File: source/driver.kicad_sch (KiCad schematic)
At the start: 49 parts, among them U2 IRS21867S, U3 IRS21867S, U4 IRS21867S, U5 TX4130L/PW2902

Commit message: Add files via upload
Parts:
- renumbered C17 to C13, C18 to C14, C19 to C15, C20 to C16, C21 to C17, C22 to C18, C23 to C19
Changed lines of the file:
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@@
   (symbol (lib_id "Device:C") (at 270.51 128.27 0) (unit 1)
     (in_bom yes) (on_board yes)
-    (property "Reference" "C22" (id 0) (at 270.51 125.73 0)
+    (property "Reference" "C18" (id 0) (at 270.51 125.73 0)
       (effects (font (size 1.27 1.27)) (justify left))
     )
@@
   (symbol (lib_id "BLDC_4-rescue:C-RESCUE-BLDC_4") (at 199.39 148.59 180) (unit 1)
     (in_bom yes) (on_board yes)
-    (property "Reference" "C18" (id 0) (at 199.39 151.13 0)
+    (property "Reference" "C14" (id 0) (at 199.39 151.13 0)
       (effects (font (size 1.27 1.27)) (justify left))
     )
@@
   (symbol (lib_id "Custom_Library:C_T491D107K016AT") (at 276.86 128.27 0) (unit 1)
     (in_bom yes) (on_board yes) (fields_autoplaced)
-    (property "Reference" "C23" (id 0) (at 280.67 126.3649 0)
+    (property "Reference" "C19" (id 0) (at 280.67 126.3649 0)
       (effects (font (size 1.27 1.27)) (justify left))
     )
@@
   (symbol (lib_id "Device:C") (at 170.18 53.34 0) (unit 1)
     (in_bom yes) (on_board yes)
-    (property "Reference" "C17" (id 0) (at 171.45 50.8 0)
+    (property "Reference" "C13" (id 0) (at 171.45 50.8 0)
       (effects (font (size 1.27 1.27)) (justify left))
     )
@@
   (symbol (lib_id "BLDC_4-rescue:C-RESCUE-BLDC_4") (at 233.68 138.43 270) (unit 1)
     (in_bom yes) (on_board yes)
-    (property "Reference" "C20" (id 0) (at 234.95 137.16 90)
+    (property "Reference" "C16" (id 0) (at 234.95 137.16 90)
       (effects (font (size 1.27 1.27)) (justify left))
     )
@@
   (symbol (lib_id "Device:C") (at 204.47 50.8 0) (unit 1)
     (in_bom yes) (on_board yes)
-    (property "Reference" "C19" (id 0) (at 204.47 48.26 0)
+    (property "Reference" "C15" (id 0) (at 204.47 48.26 0)
       (effects (font (size 1.27 1.27)) (justify left))
     )
@@
   (symbol (lib_id "Device:C") (at 264.16 128.27 0) (unit 1)
     (in_bom yes) (on_board yes)
-    (property "Reference" "C21" (id 0) (at 264.16 125.73 0)
-      (effects (font (size 1.27 1.27)) (justify left))
-    )
+    (property "Reference" "C17" (id 0) (at 264.16 125.73 0)
+      (effects (font (size 1.27 1.27)) (justify left))
+    )

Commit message: Add files via upload
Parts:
- removed C10, C12: 10u @ 50V, Capacitor_SMD:C_1206_3216Metric, symbol Device:C
- added C12, C3, C8: 10u, Capacitor_Tantalum_SMD:CP_EIA-3216-10_Kemet-I, symbol Device:C_Polarized_Small
- C10: renamed from C8; value 100n -> 1u; LCSC C14663 -> C15849
- C11: renamed from C9; value 10u @ 50V -> 10u @ 100V; footprint Capacitor_SMD:C_1206_3216Metric -> Capacitor_SMD:C_2220_5650Metric; LCSC C13585 -> C2843466
- C13: renamed from C11; value 10u @ 50V -> 10u @ 100V; footprint Capacitor_SMD:C_1206_3216Metric -> Capacitor_SMD:C_2220_5650Metric; LCSC C13585 -> C2843466
- C16: renamed from C15; value 100n -> 1u; LCSC C14663 -> C15849
- C6: renamed from C5; value 100n -> 1u; LCSC C14663 -> C15849
- renumbered C13 to C14, C14 to C15, C16 to C17, C17 to C18, C18 to C19, C19 to C20, C3 to C4, C4 to C5, C6 to C7, C7 to C9
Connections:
- net +12V: now also C12.1, C3.1, C8.1
- net GND: now also C11.1, C13.2, C12.2, C3.2, C8.2
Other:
- note added: "WATT'EVER"
- note removed: "F-Of-C"

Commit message: Add files via upload
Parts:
- removed C11: 10u @ 100V, Capacitor_SMD:C_2220_5650Metric, symbol Device:C
- renumbered C9 to C10, C10 to C11, C3 to C4, C4 to C5, C5 to C6, C6 to C7, C7 to C8, C8 to C9, R6 to R10, R7 to R11, R8 to R12, R9 to R13, R10 to R14, R11 to R15, R12 to R16, R13 to R17, R14 to R18, R15 to R19, R16 to R20, R17 to R21, R18 to R22, R19 to R23, R20 to R24, R3 to R7, R4 to R8, R5 to R9
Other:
- note removed: "combined: 20uF @ 100v"

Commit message: Add files via upload
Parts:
- removed D2, D4, D8: 1N4148WS, Diode_SMD:D_SOD-323, symbol Diode:1N4148W
- removed R19, R9: 2R, Resistor_SMD:R_0603_1608Metric, symbol Device:R
- added C10, C17, C22: 1n, Capacitor_SMD:C_0603_1608Metric, symbol Device:C
- added C11, C21: 100u@6.3V, Capacitor_SMD:C_1206_3216Metric, symbol Device:C
- added C15, C20, C9: 15n, Capacitor_SMD:C_0603_1608Metric, symbol Device:C
- added C19: 100u, Capacitor_Tantalum_SMD:CP_EIA-3528-21_Kemet-B, symbol Custom_Library:C_T491D107K016AT
- added C6: 100n, Capacitor_SMD:C_0603_1608Metric, symbol BLDC_4-rescue:C-RESCUE-BLDC_4
- added CYA0650-68UH1: 68uH, Custom:L_6.6x7.2_H5.0_CYA0650_68UH, symbol pspice:INDUCTOR
- added D2: 1N5819, Diode_SMD:D_SOD-323, symbol Diode:1N5819
- added R10, R11: 1k, Resistor_SMD:R_0603_1608Metric, symbol Device:R
- added U2: AMS1117-3.3, Package_TO_SOT_SMD:SOT-223-3_TabPin2, symbol Regulator_Linear:LM1117-3.3
- added U3, U5, U8: MC74VHC1G66, Package_TO_SOT_SMD:SOT-353_SC-70-5, symbol 74xGxx:74AHC1G4210
- added U6: XL1509-5.0E1, Package_SO:SOP-8_3.9x4.9mm_P1.27mm, symbol Custom_Library:XL1509-5.0E1
- R14: value 2R -> 1k; LCSC C22977 -> C22975
- U4: renamed from U2; value IRS21867S -> EG3112; LCSC C52290 -> C111908
- U7: renamed from U3; value IRS21867S -> EG3112; LCSC C52290 -> C111908
- U9: renamed from U4; value IRS21867S -> EG3112; LCSC C52290 -> C111908
- renumbered C7 to C12, C6 to C13, C9 to C14, C10 to C16, C11 to C18, C12 to C23, C14 to C24, C13 to C25, C15 to C26, C16 to C27, C17 to C28, C18 to C29, C19 to C30, C20 to C31, C4 to C5, C5 to C7, CYA0650-68UH1 to CYA0650-68UH2, D5 to D4, D6 to D5, D7 to D6, D9 to D7, R20 to R19, R21 to R20, R22 to R21, R23 to R22, R24 to R23, R10 to R24, R11 to R25, R7 to R8, R8 to R9, U5 to U10
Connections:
- net +12V: now also U6.1 (Vin), U6.4 (O/O)
- net GND: now also C10.2, C11.2, C15.2, C17.2, C19.2, C20.2, C21.2, C22.2, C6.1, C9.2, D2.2 (A), U2.1 (GND), U3.3 (GND), U5.3 (GND), U6.5 (GND), U6.6 (GND), U6.7 (GND), U6.8 (GND), U8.3 (GND); no longer C14.2, C16.2
- net HS1: now also C12.2, U4.6 (VS)
- net HS2: now also C18.2, U7.6 (VS); no longer R14.2
- net HS3: now also C27.2, U9.6 (VS)
- net VCC: now also C11.1, U2.2 (VO), U3.5 (VCC), U5.5 (VCC), U8.5 (VCC)
- new net: C20.1, U8.2 (X2)
- new net: C15.1, U5.2 (X2)
- new net: CYA0650-68UH1.1, D2.1 (K), U6.2 (Vout)
- new net: C9.1, U3.2 (X2)
- new net: C14.2, C16.2
- new net +5V: C19.1, C21.1, C6.2, CYA0650-68UH1.2, U2.3 (VI), U6.3 (FB)
- new net CURR_A: C10.1, R10.1, U3.1 (X1)
- new net CURR_B: C17.1, R11.1, U5.1 (X1)
- new net CURR_C: C22.1, R14.1, U8.1 (X1)
- new net CURR_FILTER: U3.4 (Q), U5.4 (Q), U8.4 (Q)
- new net C_A: R10.2
- new net C_B: R11.2
- new net C_C: R14.2
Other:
- note added: "BOARD REGULATOR"
- note added: "PCB Layout Tips (Gate Driver) Distance between high and low voltage components: It's strongly recommended to place the components tied to the floating voltage pins (VB and VS) near the respective high voltage portions of the device. Please see the Case Outline information in this datasheet for the details. Ground Plane: In order to minimize noise coupling, the ground plane should not be placed un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"
- note added: "Power stage PCB parasitic elements can contribute to large negative voltage transients at the switch node; it is recommended to limit the phase voltage negative transients. In order to avoid such conditions, it is recommended to 1) minimize the high-side emitter to low-side collector distance, and 2) minimize the low-side emitter to negative bus rail stray inductance. However, where negative VS s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"
- moved on the sheet: C13, C25, C8, R12, R13, R16, R17, R24, R25, R8, R9

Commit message: Add files via upload
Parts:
- removed C10, C22: 1n, Capacitor_SMD:C_0603_1608Metric, symbol Device:C
- removed C15, C20: 15n, Capacitor_SMD:C_0603_1608Metric, symbol Device:C
- removed R10, R11, R14: 1k, Resistor_SMD:R_0603_1608Metric, symbol Device:R
- added C14: 100n, Capacitor_SMD:C_0603_1608Metric, symbol Device:C
- C17: value 1n -> 100n; LCSC C23630 -> C14663
- C9: value 15n -> 100n; LCSC C23630 -> C14663
- U3, U5, U8: LCSC (none) -> C233641
- renumbered C11 to C10, C12 to C11, C13 to C12, C14 to C13, C16 to C15, C18 to C16, C19 to C18, C21 to C19, C23 to C20, C24 to C21, C25 to C22, C26 to C23, C27 to C24, C28 to C25, C29 to C26, C30 to C27, C31 to C28, R12 to R10, R13 to R11, R16 to R12, R17 to R13, R15 to R14, R18 to R15, R19 to R16, R20 to R17, R21 to R18, R22 to R19, R23 to R20, R24 to R21, R25 to R22
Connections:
- net GND: now also U3.2 (X2), U5.2 (X2), U8.2 (X2); no longer C17.2, C9.2
- net SENS_1: now also C9.1
- net SENS_2: now also C14.1
- net SENS_3: now also C17.1
- net CURR_A: no longer names the net of U3.1 (X1)
- net CURR_A: now also C9.2
- net CURR_B: no longer names the net of U5.1 (X1)
- net CURR_B: now also C14.2; no longer C17.1
- net CURR_C: no longer names the net of U8.1 (X1)
- net CURR_C: now also C17.2
- net CURR_FILTER renamed SENS_FILTER
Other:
- note added: "FOC KING"
- note added: "ON/OFF Voltage Filters"
- note removed: "WATT'EVER"
- moved on the sheet: R10, R11, R12, R13, R8, R9, U3

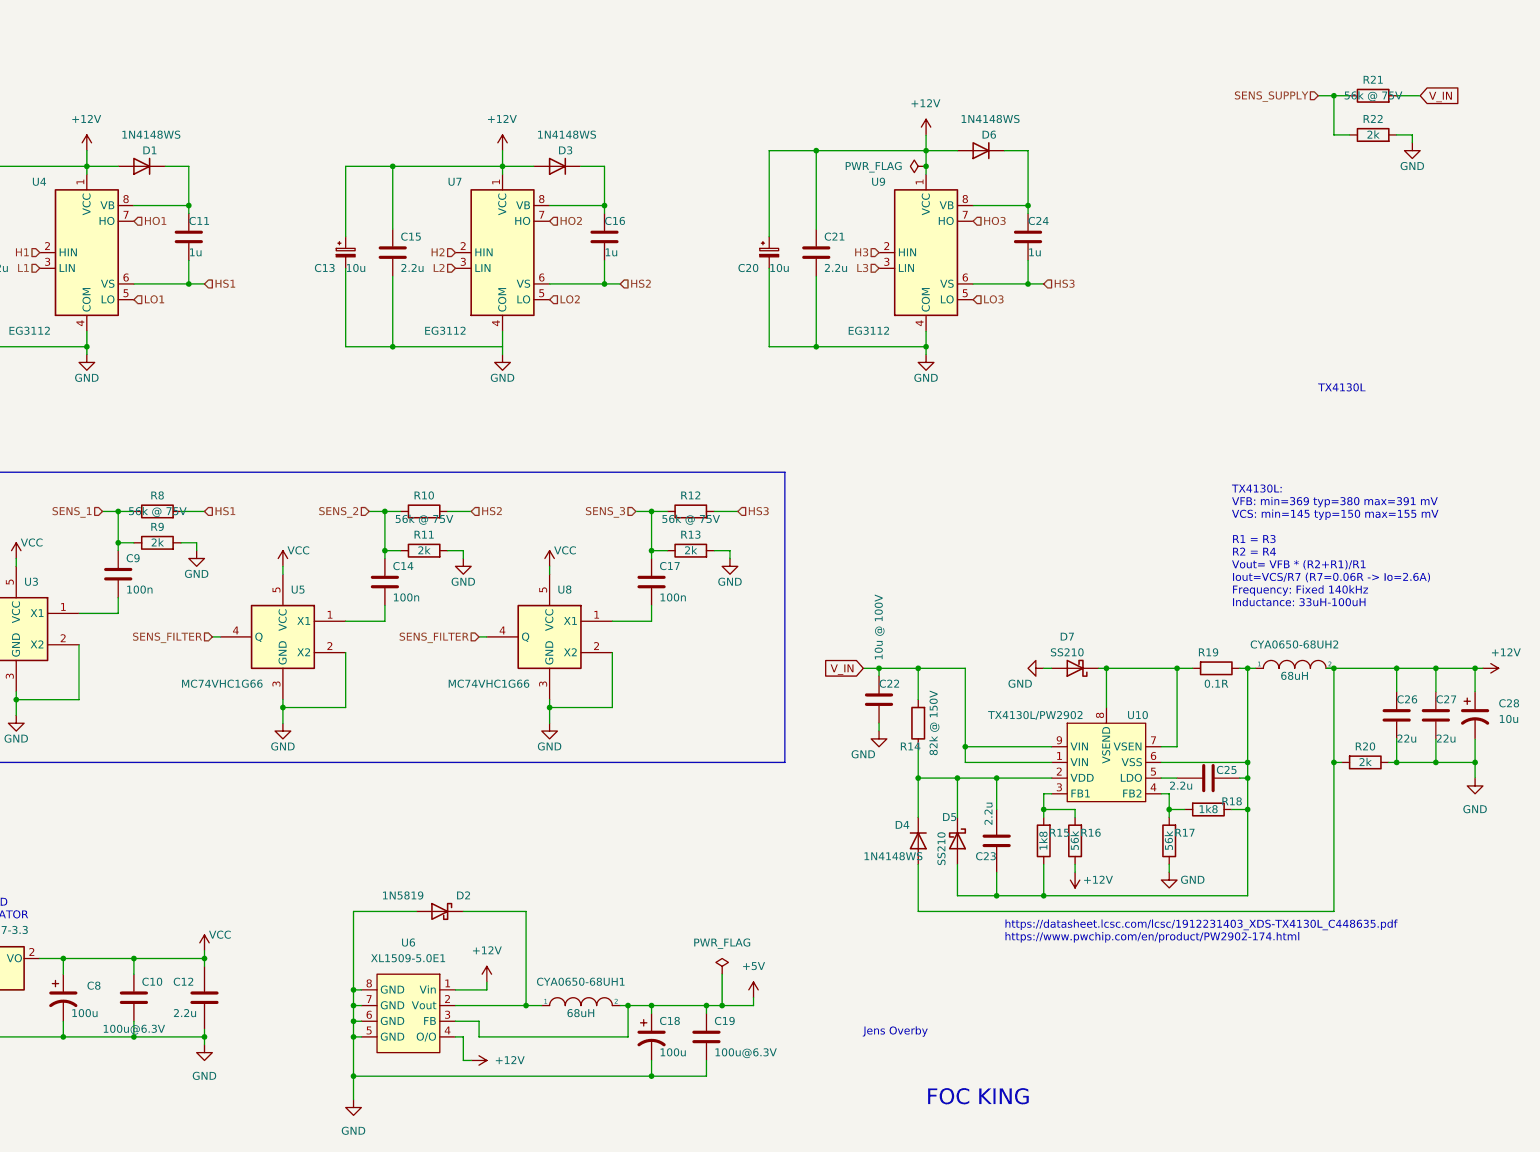
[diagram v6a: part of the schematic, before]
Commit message: 4 layer design
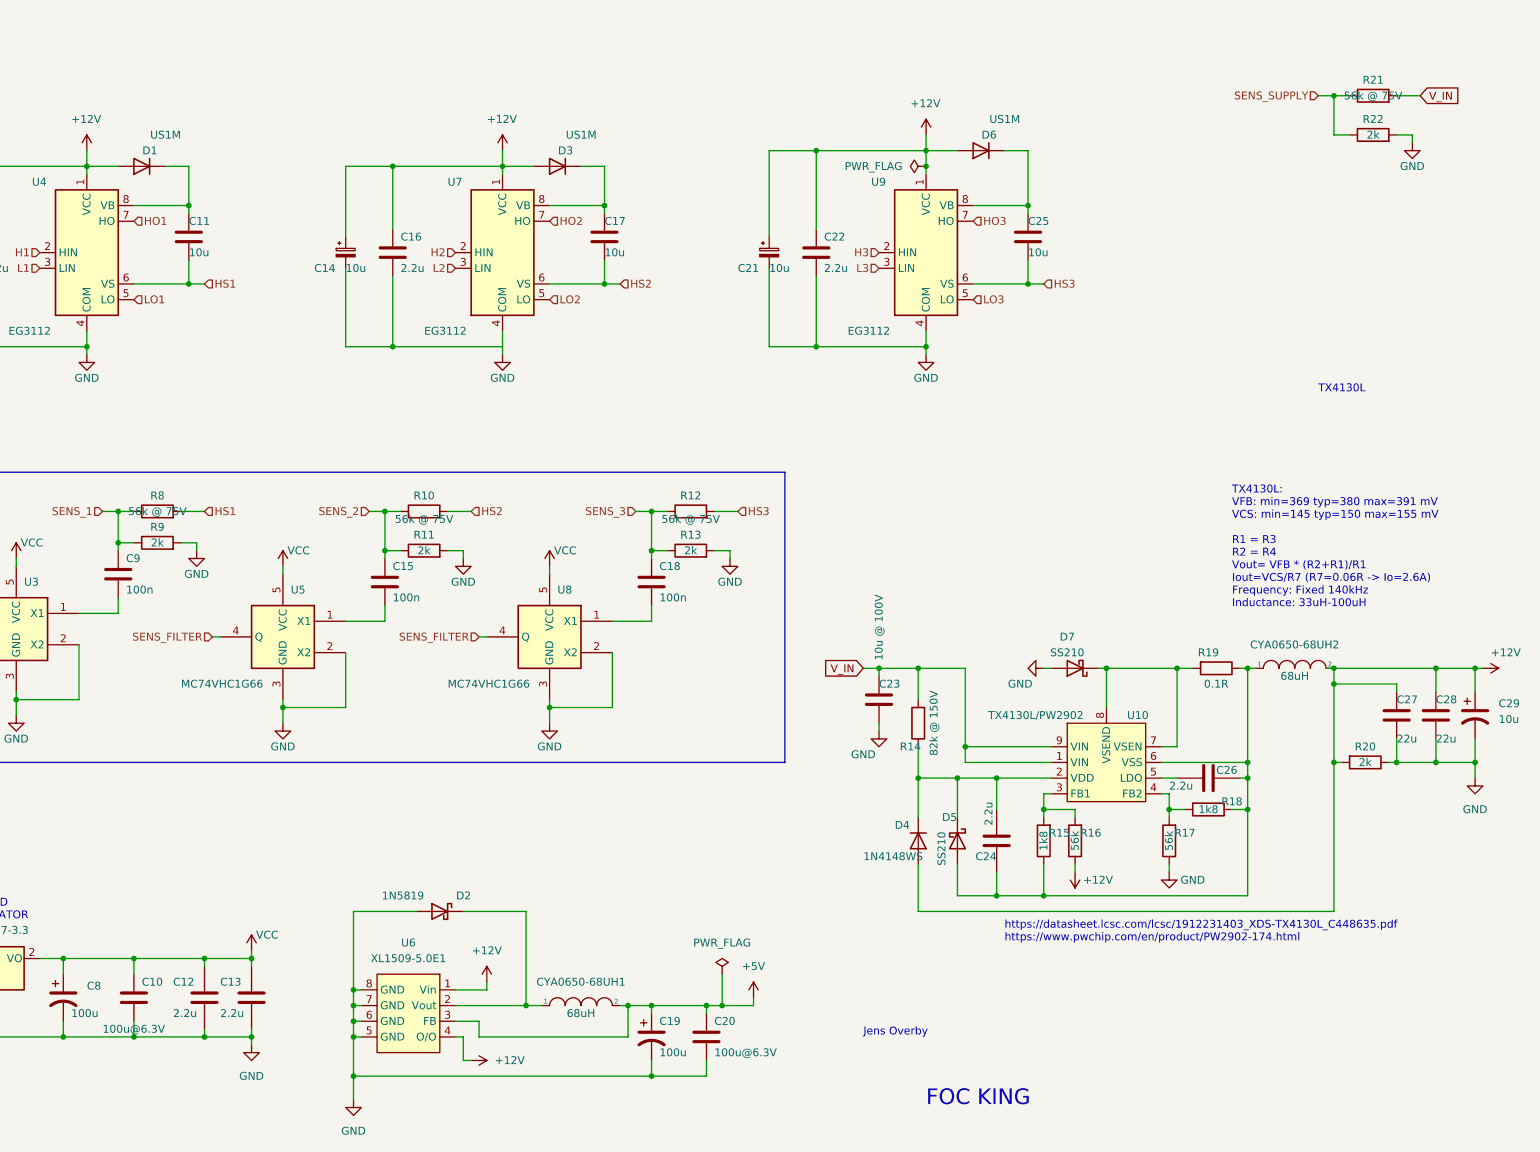
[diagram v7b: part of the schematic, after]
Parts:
- added C12: 2.2u, Capacitor_SMD:C_0603_1608Metric, symbol BLDC_4-rescue:C-RESCUE-BLDC_4
- C11: value 1u -> 10u; LCSC C15849 -> C96446
- C17: renamed from C16; value 1u -> 10u; LCSC C15849 -> C96446
- C25: renamed from C24; value 1u -> 10u; LCSC C15849 -> C96446
- D1, D3, D6: value 1N4148WS -> US1M; footprint Diode_SMD:D_SOD-323 -> Diode_SMD:D_SMA; LCSC C2128 -> C412437
- renumbered C12 to C13, C13 to C14, C14 to C15, C15 to C16, C17 to C18, C18 to C19, C19 to C20, C20 to C21, C21 to C22, C22 to C23, C23 to C24, C25 to C26, C26 to C27, C27 to C28, C28 to C29
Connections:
- net GND: now also C12.2
- net VCC: now also C12.1
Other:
- moved on the sheet: C13

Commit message: Add files via upload
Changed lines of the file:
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@@
   (junction (at 186.69 138.43) (diameter 0) (color 0 0 0 0)
   )
+  (junction (at 171.45 161.29) (diameter 0) (color 0 0 0 0)
+  )
   (wire (pts (xy 195.58 58.42) (xy 204.47 58.42))
     (stroke (width 0) (type default) (color 0 0 0 0))
@@
     (stroke (width 0) (type default) (color 0 0 0 0))
   )
+  (wire (pts (xy 171.45 165.1) (xy 171.45 161.29))
+    (stroke (width 0) (type default) (color 0 0 0 0))
+  )
   (wire (pts (xy 96.52 180.34) (xy 95.25 180.34))
     (stroke (width 0) (type default) (color 0 0 0 0))
@@
     (stroke (width 0) (type default) (color 0 0 0 0))
   )
+  (wire (pts (xy 227.33 161.29) (xy 171.45 161.29))
+    (stroke (width 0) (type default) (color 0 0 0 0))
+  )
   (wire (pts (xy 101.6 39.37) (xy 101.6 49.53))
     (stroke (width 0) (type default) (color 0 0 0 0))
@@
     (stroke (width 0) (type default) (color 0 0 0 0))
   )
-  (wire (pts (xy 227.33 152.4) (xy 227.33 153.67))
+  (wire (pts (xy 227.33 152.4) (xy 227.33 161.29))
     (stroke (width 0) (type default) (color 0 0 0 0))
   )
@@
     (stroke (width 0) (type default) (color 0 0 0 0))
   )
+  (wire (pts (xy 171.45 129.54) (xy 180.34 129.54))
+    (stroke (width 0) (type default) (color 0 0 0 0))
+  )
   (wire (pts (xy 240.03 138.43) (xy 240.03 135.89))
     (stroke (width 0) (type default) (color 0 0 0 0))
@@
     (stroke (width 0) (type default) (color 0 0 0 0))
   )
-  (wire (pts (xy 180.34 130.81) (xy 180.34 129.54))
+  (wire (pts (xy 171.45 161.29) (xy 171.45 129.54))
     (stroke (width 0) (type default) (color 0 0 0 0))
   )
@@
   (symbol (lib_id "power:+12V") (at 278.13 120.65 270) (mirror x) (unit 1)
     (in_bom yes) (on_board yes)
-    (property "Reference" "#PWR049" (id 0) (at 274.32 120.65 0)
+    (property "Reference" "#PWR048" (id 0) (at 274.32 120.65 0)
       (effects (font (size 1.27 1.27)) hide)
     )
@@
   (symbol (lib_id "power:GND") (at 276.86 138.43 0) (unit 1)
     (in_bom yes) (on_board yes)
-    (property "Reference" "#PWR048" (id 0) (at 276.86 144.78 0)
+    (property "Reference" "#PWR047" (id 0) (at 276.86 144.78 0)
       (effects (font (size 1.27 1.27)) hide)
     )
@@
   (symbol (lib_id "power:GND") (at 266.7 35.56 0) (unit 1)
     (in_bom yes) (on_board yes)
-    (property "Reference" "#PWR047" (id 0) (at 266.7 41.91 0)
+    (property "Reference" "#PWR046" (id 0) (at 266.7 41.91 0)
       (effects (font (size 1.27 1.27)) hide)
     )
@@
     (pin "1")
   )
-  (symbol (lib_id "power:GND") (at 227.33 153.67 0) (unit 1)
-    (in_bom yes) (on_board yes)
-    (property "Reference" "#PWR046" (id 0) (at 227.33 160.02 0)
-      (effects (font (size 1.27 1.27)) hide)
-    )
-    (property "Value" "GND" (id 1) (at 231.14 154.94 0))
-    (property "Footprint" "" (id 2) (at 227.33 153.67 0)
-      (effects (font (size 1.27 1.27)) hide)
-    )
-    (property "Datasheet" "" (id 3) (at 227.33 153.67 0)
-      (effects (font (size 1.27 1.27)) hide)
-    )
-    (pin "1")
-  )
   (symbol (lib_id "Device:C_Polarized_Small") (at 93.98 53.34 0) (unit 1)
     (in_bom yes) (on_board yes)
@@
     (pin "1")
   )
-  (symbol (lib_id "power:GND") (at 180.34 130.81 0) (unit 1)
+  (symbol (lib_id "power:GND") (at 171.45 165.1 0) (unit 1)
     (in_bom yes) (on_board yes)
-    (property "Reference" "#PWR041" (id 0) (at 180.34 137.16 0)
+    (property "Reference" "#PWR041" (id 0) (at 171.45 171.45 0)
       (effects (font (size 1.27 1.27)) hide)
     )
-    (property "Value" "GND" (id 1) (at 177.8 134.62 0))
-    (property "Footprint" "" (id 2) (at 180.34 130.81 0)
+    (property "Value" "GND" (id 1) (at 168.91 168.91 0))
+    (property "Footprint" "" (id 2) (at 171.45 165.1 0)
       (effects (font (size 1.27 1.27)) hide)
     )
-    (property "Datasheet" "" (id 3) (at 180.34 130.81 0)
+    (property "Datasheet" "" (id 3) (at 171.45 165.1 0)
       (effects (font (size 1.27 1.27)) hide)
     )
